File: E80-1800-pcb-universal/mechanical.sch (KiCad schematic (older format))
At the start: 4 parts

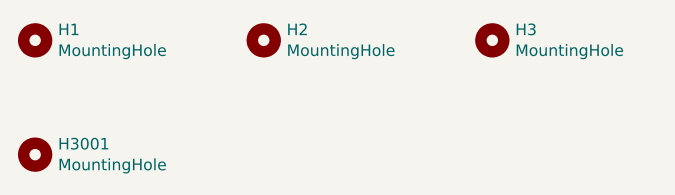
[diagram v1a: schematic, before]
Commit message: improved mounting holes
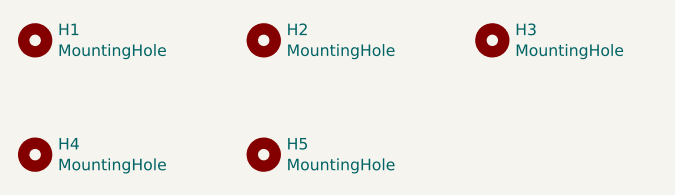
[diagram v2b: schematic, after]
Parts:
- added H5: MountingHole, MountingHole:MountingHole_4mm, symbol Mechanical:MountingHole
- renumbered H3001 to H4
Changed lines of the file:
@@
 EESchema Schematic File Version 4
-LIBS:E80-1800-pcb-universal-cache
 EELAYER 30 0
 EELAYER END
@@
 $EndComp
 $Comp
-L Mechanical:MountingHole H3001
+L Mechanical:MountingHole H4
 U 1 1 5F3A9BF5
 P 1000 1500
-F 0 "H3001" H 1100 1546 50  0000 L CNN
+F 0 "H4" H 1100 1546 50  0000 L CNN
 F 1 "MountingHole" H 1100 1455 50  0000 L CNN
 F 2 "MountingHole:MountingHole_4mm" H 1000 1500 50  0001 C CNN
@@
 	1    0    0    -1
 $EndComp
+$Comp
+L Mechanical:MountingHole H5
+U 1 1 5F5E9471
+P 2000 1500
+F 0 "H5" H 2100 1546 50  0000 L CNN
+F 1 "MountingHole" H 2100 1455 50  0000 L CNN
+F 2 "MountingHole:MountingHole_4mm" H 2000 1500 50  0001 C CNN
+F 3 "~" H 2000 1500 50  0001 C CNN
+	1    2000 1500
+	1    0    0    -1
+$EndComp
